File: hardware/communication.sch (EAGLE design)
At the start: 44 parts, among them J1 MICRO_USB_B_HIROSE_ZX62-B-5PA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, U1 ES920LR3, U2 NJM12888F, X1 FA-238

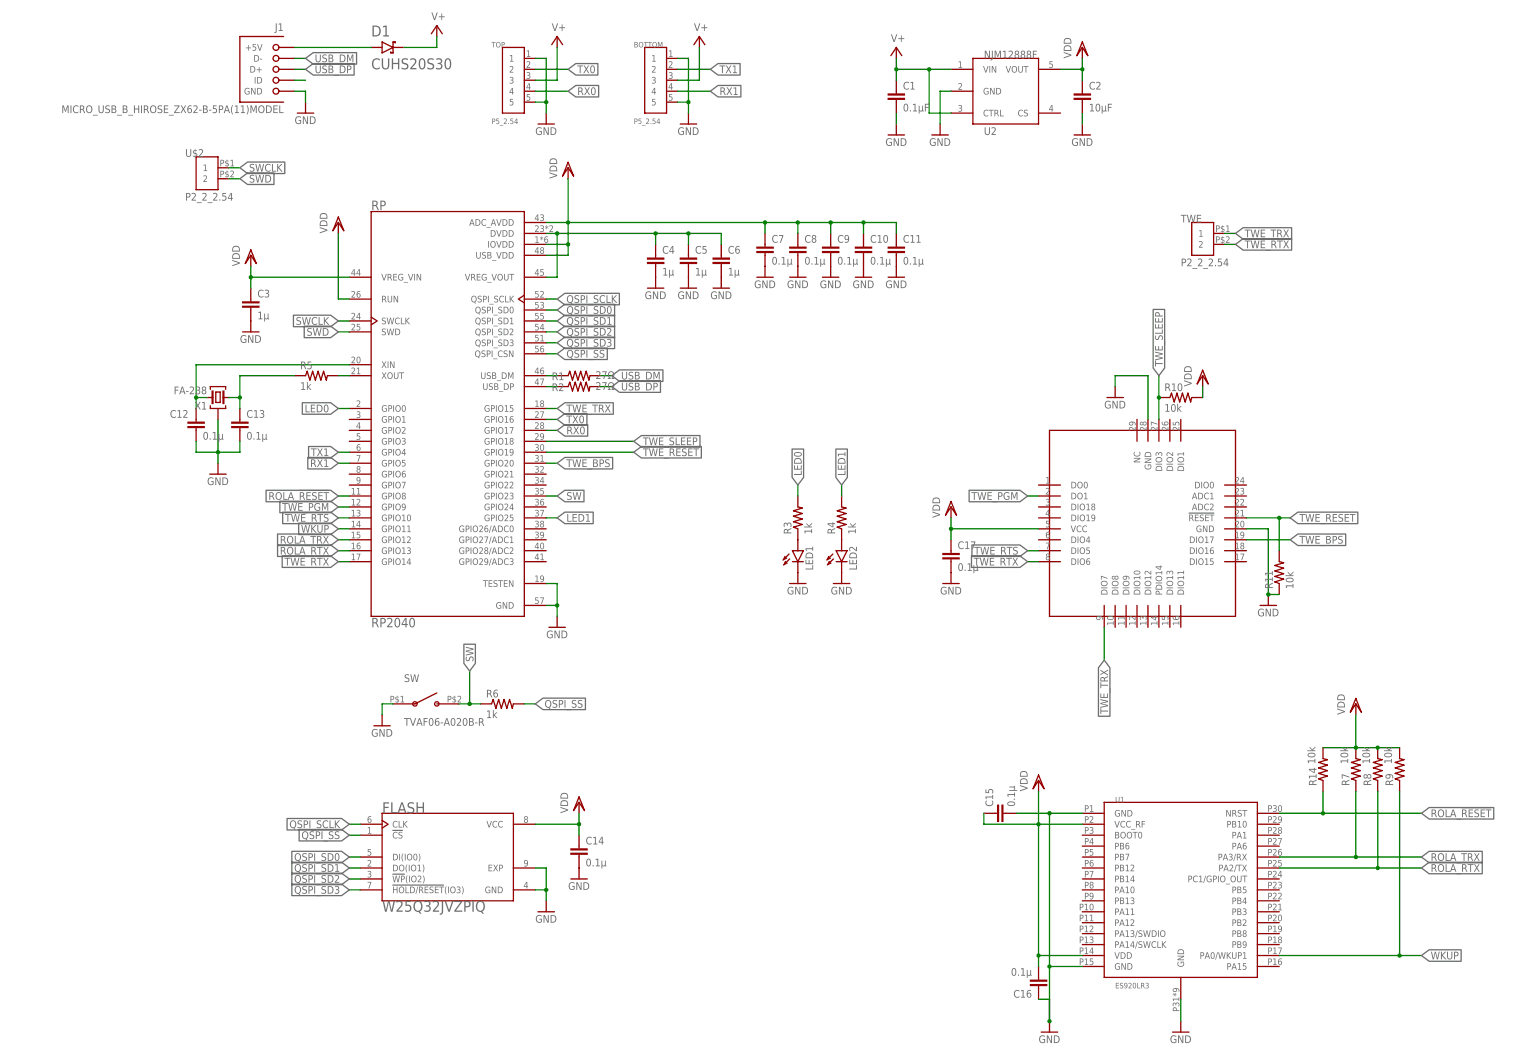
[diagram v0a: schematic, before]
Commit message: LiPo回路修正，新LoRa
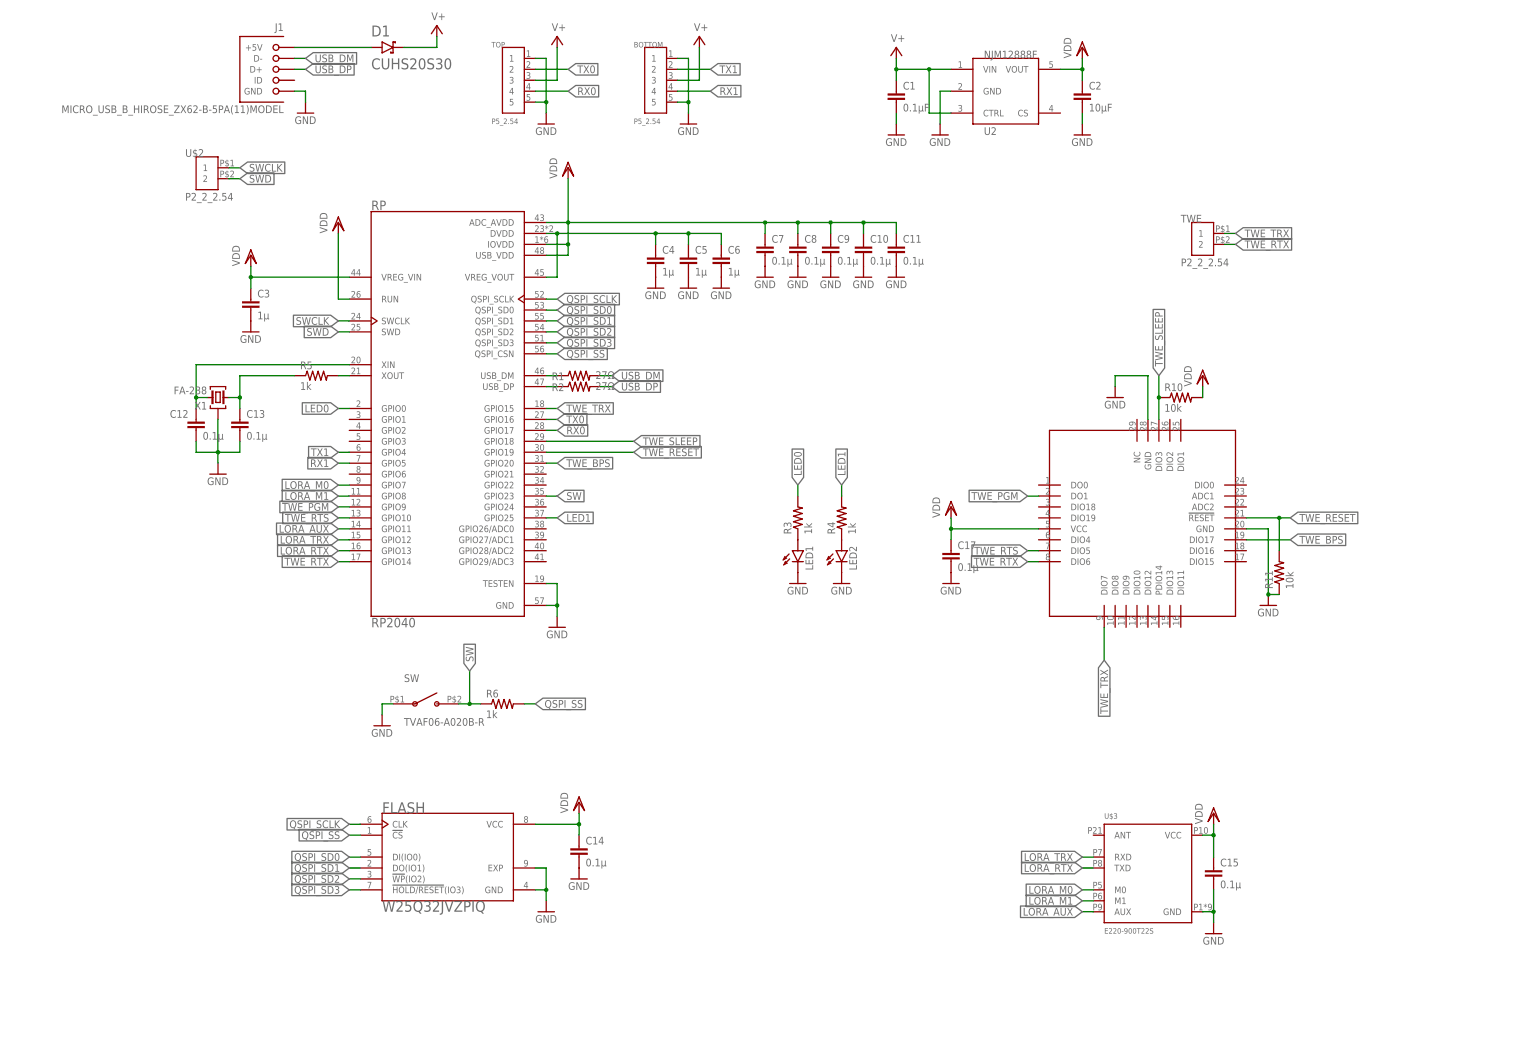
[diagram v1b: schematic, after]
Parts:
- removed C16: 0.1µ, rcl:C-EUC0402
- removed R14, R7, R8, R9: 10k, rcl:R-US_R0402
- removed U1: ES920LR3, lora:ES920LR3
- added U$3: E220-900T22S, lora:E220-900T22S
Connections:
- removed net N$5: J1.ID
- removed net ROLA_!RESET!: R14.1, RP.GPIO8, U1.NRST
- removed net ROLA_RTX: R8.1, RP.GPIO13, U1.PA2/TX
- removed net ROLA_TRX: R7.1, RP.GPIO12, U1.PA3/RX
- removed net WKUP: R9.1, RP.GPIO11, U1.PA0/WKUP1
- new net LORA_AUX: RP.GPIO11, U$3.AUX
- new net LORA_M0: RP.GPIO7, U$3.M0
- new net LORA_M1: RP.GPIO8, U$3.M1
- new net LORA_RTX: RP.GPIO13, U$3.TXD
- new net LORA_TRX: RP.GPIO12, U$3.RXD
- net GND: now also U$3.GND; no longer C16.1, U1.GND, U1.GND@1, U1.GND@2
- net VDD: now also U$3.VCC; no longer C16.2, R14.2, R7.2, R8.2, R9.2, U1.VCC_RF, U1.VDD
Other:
- moved on the sheet: C15

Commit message: ベタ・シルク調整
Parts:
- renumbered U$3 to U1
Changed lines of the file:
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@@
 <part name="VDD9" library="supply1" library_urn="urn:adsk.eagle:library:371" deviceset="VDD" device=""/>
 <part name="TWE" library="pins" deviceset="P2_2_2.54" device=""/>
-<part name="U$3" library="lora" deviceset="E220-900T22S" device=""/>
+<part name="U1" library="lora" deviceset="E220-900T22S" device=""/>
 <part name="GND6" library="supply1" library_urn="urn:adsk.eagle:library:371" deviceset="GND" device=""/>
 <part name="VDD10" library="supply1" library_urn="urn:adsk.eagle:library:371" deviceset="VDD" device=""/>
@@
 <attribute name="VALUE" x="226.06" y="129.54" size="1.778" layer="96"/>
 </instance>
-<instance part="U$3" gate="G$1" x="218.44" y="-10.16" smashed="yes">
+<instance part="U1" gate="G$1" x="218.44" y="-10.16" smashed="yes">
 <attribute name="NAME" x="208.28" y="2.54" size="1.27" layer="95" align="top-left"/>
 <attribute name="VALUE" x="208.28" y="-25.4" size="1.27" layer="96"/>
@@
 </segment>
 <segment>
-<pinref part="U$3" gate="G$1" pin="GND"/>
+<pinref part="U1" gate="G$1" pin="GND"/>
 <wire x1="231.14" y1="-20.32" x2="233.68" y2="-20.32" width="0.1524" layer="91"/>
 <wire x1="233.68" y1="-20.32" x2="233.68" y2="-22.86" width="0.1524" layer="91"/>
@@
 </segment>
 <segment>
-<pinref part="U$3" gate="G$1" pin="VCC"/>
+<pinref part="U1" gate="G$1" pin="VCC"/>
 <wire x1="231.14" y1="-2.54" x2="233.68" y2="-2.54" width="0.1524" layer="91"/>
 <wire x1="233.68" y1="-2.54" x2="233.68" y2="0" width="0.1524" layer="91"/>
@@
 <net name="LORA_TRX" class="0">
 <segment>
-<pinref part="U$3" gate="G$1" pin="RXD"/>
+<pinref part="U1" gate="G$1" pin="RXD"/>
 <wire x1="205.74" y1="-7.62" x2="203.2" y2="-7.62" width="0.1524" layer="91"/>
 <label x="203.2" y="-7.62" size="1.778" layer="95" rot="R180" xref="yes"/>
@@
 <net name="LORA_RTX" class="0">
 <segment>
-<pinref part="U$3" gate="G$1" pin="TXD"/>
+<pinref part="U1" gate="G$1" pin="TXD"/>
 <wire x1="205.74" y1="-10.16" x2="203.2" y2="-10.16" width="0.1524" layer="91"/>
 <label x="203.2" y="-10.16" size="1.778" layer="95" rot="R180" xref="yes"/>
@@
 <net name="LORA_M0" class="0">
 <segment>
-<pinref part="U$3" gate="G$1" pin="M0"/>
+<pinref part="U1" gate="G$1" pin="M0"/>
 <wire x1="205.74" y1="-15.24" x2="203.2" y2="-15.24" width="0.1524" layer="91"/>
 <label x="203.2" y="-15.24" size="1.778" layer="95" rot="R180" xref="yes"/>
@@
 <net name="LORA_M1" class="0">
 <segment>
-<pinref part="U$3" gate="G$1" pin="M1"/>
+<pinref part="U1" gate="G$1" pin="M1"/>
 <wire x1="205.74" y1="-17.78" x2="203.2" y2="-17.78" width="0.1524" layer="91"/>
 <label x="203.2" y="-17.78" size="1.778" layer="95" rot="R180" xref="yes"/>
@@
 <net name="LORA_AUX" class="0">
 <segment>
-<pinref part="U$3" gate="G$1" pin="AUX"/>
+<pinref part="U1" gate="G$1" pin="AUX"/>
 <wire x1="205.74" y1="-20.32" x2="203.2" y2="-20.32" width="0.1524" layer="91"/>
 <label x="203.2" y="-20.32" size="1.778" layer="95" rot="R180" xref="yes"/>
